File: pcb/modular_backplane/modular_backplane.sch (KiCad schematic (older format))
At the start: 50 parts, among them U1 DMP3028LK3-13, U2 DMP3028LK3-13, U3 PREC002SAAN-RC, U4 NTD4969NT4G, U5 PREC002SAAN-RC, U6 NTD4969NT4G

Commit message: updates
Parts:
- removed boardToCard1, boardToCard2, boardToCard3, boardToCard4, boardToCard5, boardToCard6, boardToCard7, boardToCard8, boardToCard9: SSQ-104-02-T-S-RA, backplane:SSQ-104-02-T-S-RA, symbol backplane_Library:SSQ-104-02-T-S-RA
- added R15, R16: 10K, Resistor_SMD:R_1206_3216Metric_Pad1.42x1.75mm_HandSolder, symbol Device:R
- added boardToCard1, boardToCard2, boardToCard3, boardToCard4, boardToCard5, boardToCard6, boardToCard7, boardToCard8, boardToCard9: SSQ-108-02-T-S-RA, backplane:SSQ-108-02-T-S-RA, symbol backplane_Library:SSQ-108-02-T-S-RA
- added i2cPins1: PREC002SAAN-RC, backplane:PREC002SAAN-RC, symbol backplane_Library:PREC002SAAN-RC
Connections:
- net labels added: scl, sda
- wire segments 229 -> 337
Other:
- note added: "external card connectors"
- note added: "i2c"

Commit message: updates
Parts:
- removed boardToCard1, boardToCard2, boardToCard3, boardToCard4, boardToCard5, boardToCard6, boardToCard7, boardToCard8, boardToCard9: SSQ-108-02-T-S-RA, backplane:SSQ-108-02-T-S-RA, symbol backplane_Library:SSQ-108-02-T-S-RA
- added U7: PREC027DAAN-RC, backplane:PREC027DAAN-RC, symbol backplane_Library:PREC027DAAN-RC
- added card1, card2, card3, card4, card5, card6, card7, card8, card9: PPPC072LJBN-RC, backplane:PPPC072LJBN-RC, symbol backplane_Library:PPPC072LJBN-RC
- R15, R16: value 10K -> 4.7K
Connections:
- net labels added: header1Gpio1, header1Gpio2, header1Gpio3, header1Gpio4, header1Gpio5, header1Gpio6, header2Gpio1, header2Gpio2, header2Gpio3, header2Gpio4, header2Gpio5, header2Gpio6, header3Gpio1, header3Gpio2, header3Gpio3, header3Gpio4, header3Gpio5, header3Gpio6, header4Gpio1, header4Gpio2, header4Gpio3, header4Gpio4, header4Gpio5, header4Gpio6, header5Gpio1, header5Gpio2, header5Gpio3, header5Gpio4, header5Gpio5, header5Gpio6, header6Gpio1, header6Gpio2, header6Gpio3, header6Gpio4, header6Gpio5, header6Gpio6, header7Gpio1, header7Gpio2, header7Gpio3, header7Gpio4, header7Gpio5, header7Gpio6, header8Gpio1, header8Gpio2, header8Gpio3, header8Gpio4, header8Gpio5, header8Gpio6, header9Gpio1, header9Gpio2, header9Gpio3, header9Gpio4, header9Gpio5, header9Gpio6
- wire segments 337 -> 481

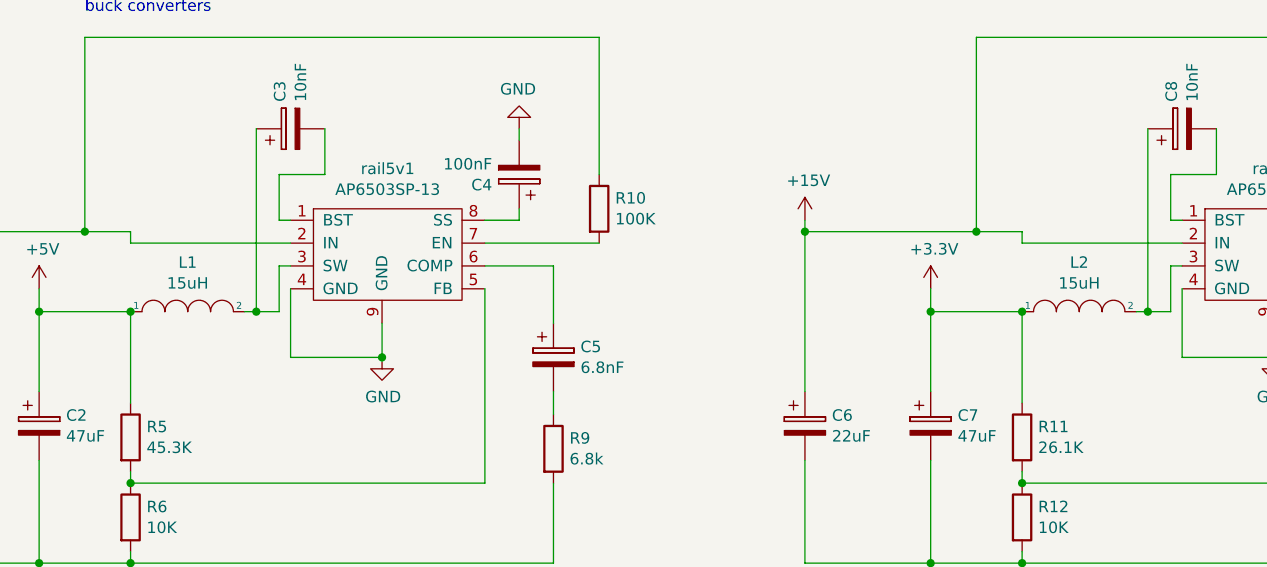
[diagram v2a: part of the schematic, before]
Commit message: layers
i added plane layers to prepare for routing
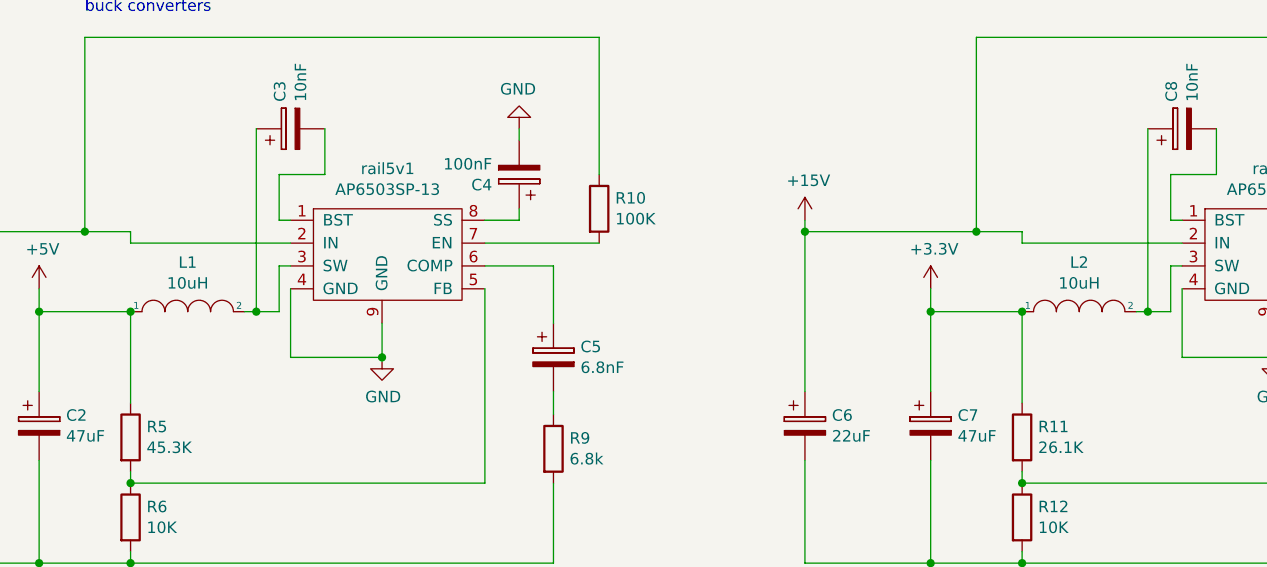
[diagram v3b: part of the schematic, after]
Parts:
- L1, L2: value 15uH -> 10uH; footprint backplane:6100-150K-RC -> backplane:RCH8011NP-100L
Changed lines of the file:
@@
 P 4900 2050
 F 0 "L1" H 4900 2265 50  0000 C CNN
-F 1 "15uH" H 4900 2174 50  0000 C CNN
-F 2 "backplane:6100-150K-RC" H 4900 2050 50  0001 C CNN
+F 1 "10uH" H 4900 2174 50  0000 C CNN
+F 2 "backplane:RCH8011NP-100L" H 4900 2050 50  0001 C CNN
 F 3 "~" H 4900 2050 50  0001 C CNN
 	1    4900 2050
@@
 P 8800 2050
 F 0 "L2" H 8800 2265 50  0000 C CNN
-F 1 "15uH" H 8800 2174 50  0000 C CNN
-F 2 "backplane:6100-150K-RC" H 8800 2050 50  0001 C CNN
+F 1 "10uH" H 8800 2174 50  0000 C CNN
+F 2 "backplane:RCH8011NP-100L" H 8800 2050 50  0001 C CNN
 F 3 "~" H 8800 2050 50  0001 C CNN
 	1    8800 2050

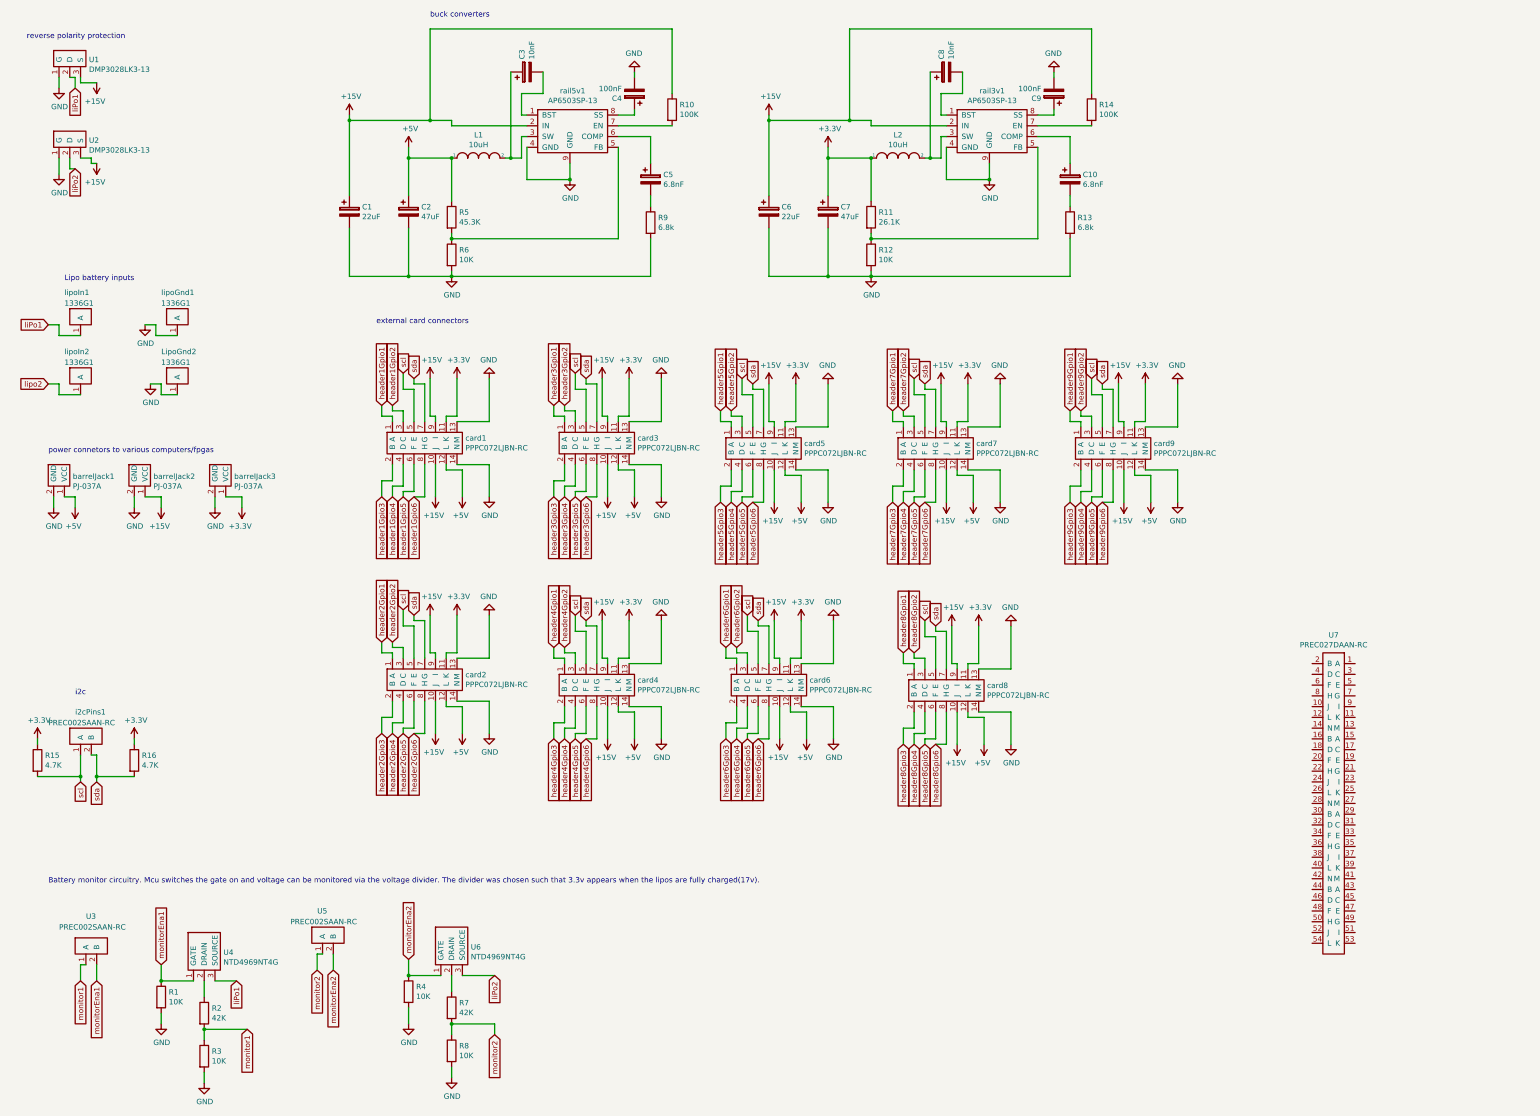
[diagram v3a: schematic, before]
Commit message: added 12v line
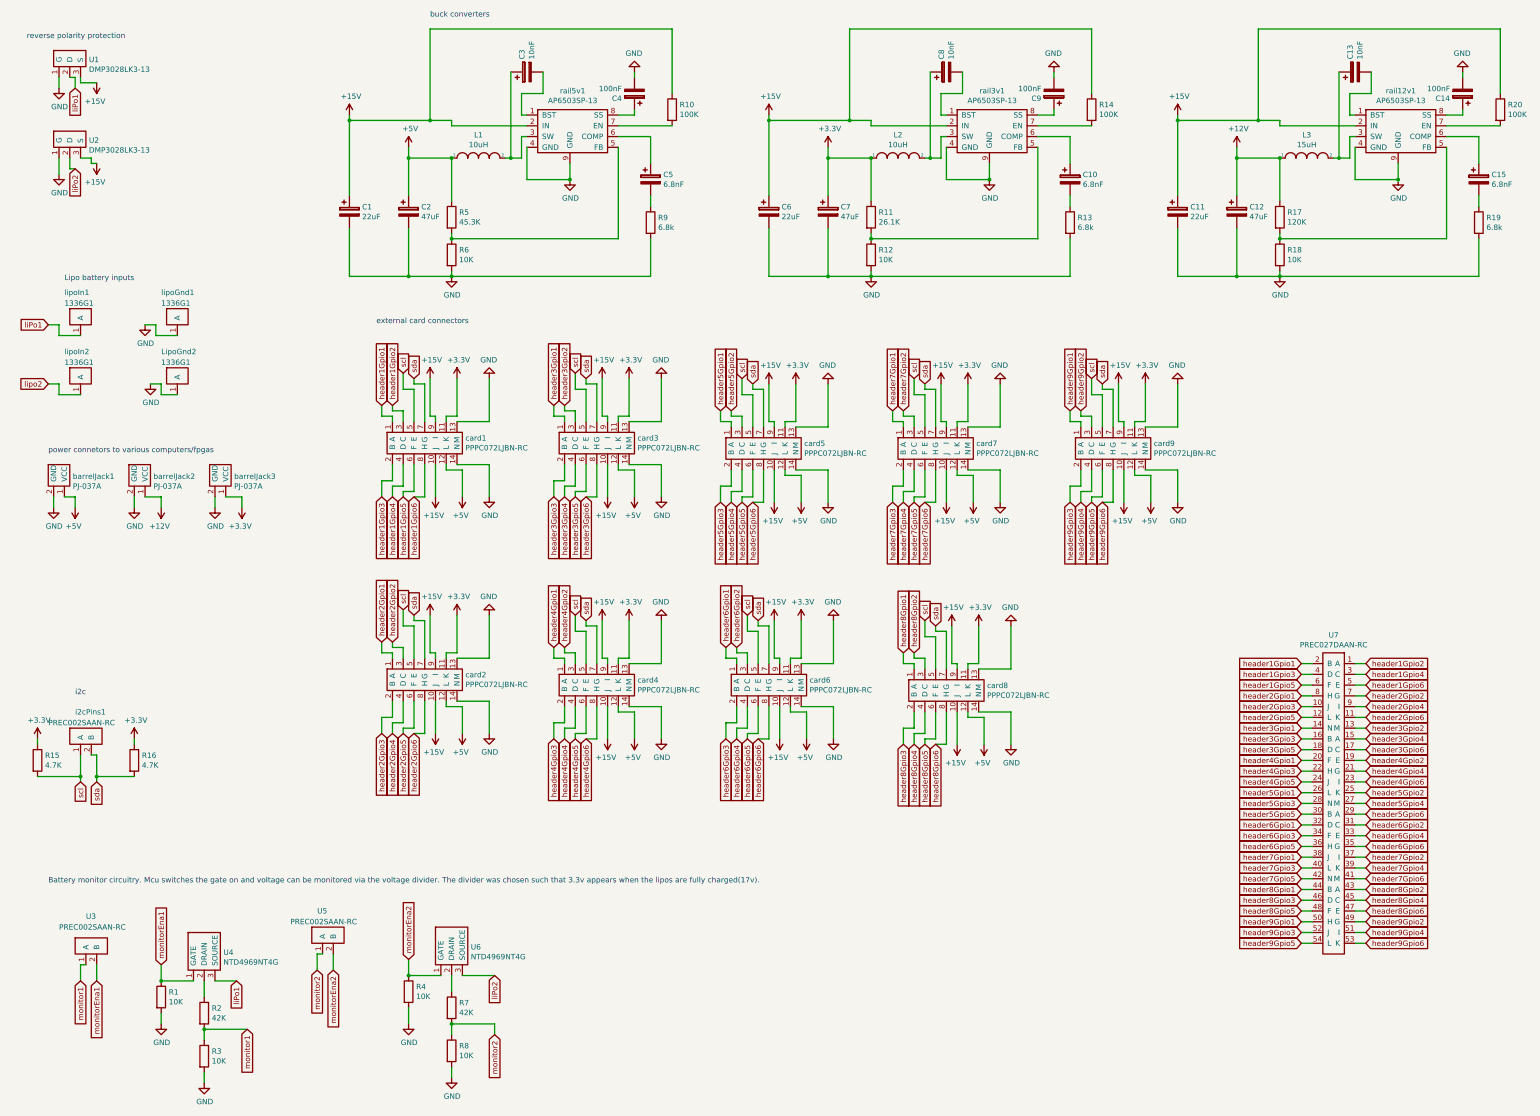
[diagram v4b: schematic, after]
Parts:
- added C11: 22uF, backplane:865090442004, symbol Device:CP
- added C12: 47uF, backplane:865090449007, symbol Device:CP
- added C13: 10nF, Capacitor_SMD:C_1206_3216Metric_Pad1.42x1.75mm_HandSolder, symbol Device:CP
- added C14: 100nF, Capacitor_SMD:C_1206_3216Metric_Pad1.42x1.75mm_HandSolder, symbol Device:CP
- added C15: 6.8nF, Capacitor_SMD:C_1206_3216Metric_Pad1.42x1.75mm_HandSolder, symbol Device:CP
- added L3: 15uH, backplane:6100-150K-RC, symbol pspice:INDUCTOR
- added R17: 120K, Resistor_SMD:R_1206_3216Metric_Pad1.42x1.75mm_HandSolder, symbol Device:R
- added R18: 10K, Resistor_SMD:R_1206_3216Metric_Pad1.42x1.75mm_HandSolder, symbol Device:R
- added R19: 6.8k, Resistor_SMD:R_1206_3216Metric_Pad1.42x1.75mm_HandSolder, symbol Device:R
- added R20: 100K, Resistor_SMD:R_1206_3216Metric_Pad1.42x1.75mm_HandSolder, symbol Device:R
- added rail12v1: AP6503SP-13, backplane:AP6503SP-13, symbol backplane_Library:AP6503SP-13
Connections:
- net +15V: now also C11.1, R20.1, rail12v1.2 (IN); no longer barrelJack2.1 (VCC)
- net GND: now also C11.2, C12.2, C14.2, R18.2, R19.2, rail12v1.4 (GND), rail12v1.9 (GND)
- net header1Gpio1: now also U7.2 (B)
- net header1Gpio2: now also U7.1 (A)
- net header1Gpio3: now also U7.4 (D)
- net header1Gpio4: now also U7.3 (C)
- net header1Gpio5: now also U7.6 (F)
- net header1Gpio6: now also U7.5 (E)
- net header2Gpio1: now also U7.8 (H)
- net header2Gpio2: now also U7.7 (G)
- net header2Gpio3: now also U7.10 (J)
- net header2Gpio4: now also U7.9 (I)
- net header2Gpio5: now also U7.12 (L)
- net header2Gpio6: now also U7.11 (K)
- net header3Gpio1: now also U7.14 (N)
- net header3Gpio2: now also U7.13 (M)
- net header3Gpio3: now also U7.16 (B)
- net header3Gpio4: now also U7.15 (A)
- net header3Gpio5: now also U7.18 (D)
- net header3Gpio6: now also U7.17 (C)
- net header4Gpio1: now also U7.20 (F)
- net header4Gpio2: now also U7.19 (E)
- net header4Gpio3: now also U7.22 (H)
- net header4Gpio4: now also U7.21 (G)
- net header4Gpio5: now also U7.24 (J)
- net header4Gpio6: now also U7.23 (I)
- net header5Gpio1: now also U7.26 (L)
- net header5Gpio2: now also U7.25 (K)
- net header5Gpio3: now also U7.28 (N)
- net header5Gpio4: now also U7.27 (M)
- net header5Gpio5: now also U7.30 (B)
- net header5Gpio6: now also U7.29 (A)
- net header6Gpio1: now also U7.32 (D)
- net header6Gpio2: now also U7.31 (C)
- net header6Gpio3: now also U7.34 (F)
- net header6Gpio4: now also U7.33 (E)
- net header6Gpio5: now also U7.36 (H)
- net header6Gpio6: now also U7.35 (G)
- net header7Gpio1: now also U7.38 (J)
- net header7Gpio2: now also U7.37 (I)
- net header7Gpio3: now also U7.40 (L)
- net header7Gpio4: now also U7.39 (K)
- net header7Gpio5: now also U7.42 (N)
- net header7Gpio6: now also U7.41 (M)
- net header8Gpio1: now also U7.44 (B)
- net header8Gpio2: now also U7.43 (A)
- net header8Gpio3: now also U7.46 (D)
- net header8Gpio4: now also U7.45 (C)
- net header8Gpio5: now also U7.48 (F)
- net header8Gpio6: now also U7.47 (E)
- net header9Gpio1: now also U7.50 (H)
- net header9Gpio2: now also U7.49 (G)
- net header9Gpio3: now also U7.52 (J)
- net header9Gpio4: now also U7.51 (I)
- net header9Gpio5: now also U7.54 (L)
- net header9Gpio6: now also U7.53 (K)
- new net: C13.2, rail12v1.1 (BST)
- new net: C13.1, L3.2, rail12v1.3 (SW)
- new net: R17.2, R18.1, rail12v1.5 (FB)
- new net: C15.1, rail12v1.6 (COMP)
- new net: R20.2, rail12v1.7 (EN)
- new net: C14.1, rail12v1.8 (SS)
- new net: C15.2, R19.1
- new net +12V: C12.1, L3.1, R17.1, barrelJack2.1 (VCC)

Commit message: done
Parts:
- removed R4, R8: 10K, Resistor_SMD:R_1206_3216Metric_Pad1.42x1.75mm_HandSolder, symbol Device:R
- removed R7: 42K, Resistor_SMD:R_1206_3216Metric_Pad1.42x1.75mm_HandSolder, symbol Device:R
- removed U5: PREC002SAAN-RC, backplane:PREC002SAAN-RC, symbol backplane_Library:PREC002SAAN-RC
- removed U6: NTD4969NT4G, backplane:NTD4969NT4G, symbol backplane_Library:NTD4969NT4G
- removed U7: PREC027DAAN-RC, backplane:PREC027DAAN-RC, symbol backplane_Library:PREC027DAAN-RC
- removed card1: PPPC072LJBN-RC, backplane:PPPC072LJBN-RC, symbol backplane_Library:PPPC072LJBN-RC
- added U5: PREC024DAAN-RC, backplane:PREC024DAAN-RC, symbol backplane_Library:PREC024DAAN-RC
- L3: value 15uH -> 10uH; footprint backplane:6100-150K-RC -> backplane:RCH8011NP-100L
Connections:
- net lipo2 is gone; now on net liPo2: lipoIn2.1 (A)
- net +15V: now also U4.3 (SOURCE)
- net GND: now also card2.5 (E), card2.7 (G), card3.5 (E), card3.7 (G), card4.5 (E), card4.7 (G), card5.5 (E), card5.7 (G), card6.5 (E), card6.7 (G), card7.5 (E), card7.7 (G), card8.5 (E), card8.7 (G), card9.5 (E), card9.7 (G); no longer card2.13 (M), card2.14 (N), card3.13 (M), card3.14 (N), card4.13 (M), card4.14 (N), card5.13 (M), card5.14 (N), card6.13 (M), card6.14 (N), card7.13 (M), card7.14 (N), card8.13 (M), card8.14 (N), card9.13 (M), card9.14 (N)
- net header2Gpio1: now also U5.10 (J)
- net header2Gpio2: now also U5.12 (L)
- net header2Gpio3: now also U5.8 (H)
- net header2Gpio4: now also U5.6 (F)
- net header2Gpio5: now also U5.4 (D)
- net header2Gpio6: now also U5.2 (B)
- net header3Gpio1: now also U5.22 (H)
- net header3Gpio2: now also U5.24 (J)
- net header3Gpio3: now also U5.20 (F)
- net header3Gpio4: now also U5.18 (D)
- net header3Gpio5: now also U5.16 (B)
- net header3Gpio6: now also U5.14 (N)
- net header4Gpio1: now also U5.34 (F)
- net header4Gpio2: now also U5.36 (H)
- net header4Gpio3: now also U5.32 (D)
- net header4Gpio4: now also U5.30 (B)
- net header4Gpio5: now also U5.28 (N)
- net header4Gpio6: now also U5.26 (L)
- net header5Gpio1: now also U5.46 (D)
- net header5Gpio2: now also U5.48 (F)
- net header5Gpio3: now also U5.44 (B)
- net header5Gpio4: now also U5.42 (N)
- net header5Gpio5: now also U5.40 (L)
- net header5Gpio6: now also U5.38 (J)
- net header6Gpio1: now also U5.3 (C)
- net header6Gpio2: now also U5.1 (A)
- net header6Gpio3: now also U5.5 (E)
- net header6Gpio4: now also U5.7 (G)
- net header6Gpio5: now also U5.9 (I)
- net header6Gpio6: now also U5.11 (K)
- net header7Gpio1: now also U5.15 (A)
- net header7Gpio2: now also U5.13 (M)
- net header7Gpio3: now also U5.17 (C)
- net header7Gpio4: now also U5.19 (E)
- net header7Gpio5: now also U5.21 (G)
- net header7Gpio6: now also U5.23 (I)
- net header8Gpio1: now also U5.27 (M)
- net header8Gpio2: now also U5.25 (K)
- net header8Gpio3: now also U5.29 (A)
- net header8Gpio4: now also U5.31 (C)
- net header8Gpio5: now also U5.33 (E)
- net header8Gpio6: now also U5.35 (G)
- net header9Gpio1: now also U5.39 (K)
- net header9Gpio2: now also U5.37 (I)
- net header9Gpio3: now also U5.41 (M)
- net header9Gpio4: now also U5.43 (A)
- net header9Gpio5: now also U5.45 (C)
- net header9Gpio6: now also U5.47 (E)
- net liPo1: no longer U4.3 (SOURCE)
- net scl: now also card2.14 (N), card3.14 (N), card4.14 (N), card5.14 (N), card6.14 (N), card7.14 (N), card8.14 (N), card9.14 (N); no longer card2.5 (E), card3.5 (E), card4.5 (E), card5.5 (E), card6.5 (E), card7.5 (E), card8.5 (E), card9.5 (E)
- net sda: now also card2.13 (M), card3.13 (M), card4.13 (M), card5.13 (M), card6.13 (M), card7.13 (M), card8.13 (M), card9.13 (M); no longer card2.7 (G), card3.7 (G), card4.7 (G), card5.7 (G), card6.7 (G), card7.7 (G), card8.7 (G), card9.7 (G)
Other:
- moved on the sheet: card3, card5, card7, card9

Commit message: motordriver finished
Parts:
- added U6, U7, U8, U9: mountingHole, backplane:mountingHole, symbol backplane_Library:mountingHole
- renumbered U3 to monitorPins1
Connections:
- net GND: now also U6.1 (A), U7.1 (A), U8.1 (A), U9.1 (A)
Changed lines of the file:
@@
 Battery monitor circuitry. Mcu switches the gate on and voltage can be monitored via the voltage divider. The divider was chosen such that 3.3v appears when the lipos are fully charged(17v).
 $Comp
-L backplane_Library:PREC002SAAN-RC U3
+L backplane_Library:PREC002SAAN-RC monitorPins1
 U 1 1 5C718C1D
 P 1300 9550
-F 0 "U3" H 1250 10000 50  0000 L CNN
+F 0 "monitorPins1" H 1250 10000 50  0000 L CNN
 F 1 "PREC002SAAN-RC" H 1000 9900 50  0000 L CNN
 F 2 "backplane:PREC002SAAN-RC" H 1300 9550 50  0001 C CNN
@@
 	9150 6350 9150 6450
 Connection ~ 9100 6350
+$Comp
+L backplane_Library:mountingHole U6
+U 1 1 5C4894C8
+P 11050 4100
+F 0 "U6" H 11128 4115 50  0000 L CNN
+F 1 "mountingHole" H 11128 4024 50  0000 L CNN
+F 2 "backplane:mountingHole" H 11050 4100 50  0001 C CNN
+F 3 "" H 11050 4100 50  0001 C CNN
+	1    11050 4100
+	1    0    0    -1
+$EndComp
+$Comp
+L backplane_Library:mountingHole U8
+U 1 1 5C489687
+P 11850 4100
+F 0 "U8" H 11928 4115 50  0000 L CNN
+F 1 "mountingHole" H 11928 4024 50  0000 L CNN
+F 2 "backplane:mountingHole" H 11850 4100 50  0001 C CNN
+F 3 "" H 11850 4100 50  0001 C CNN
+	1    11850 4100
+	1    0    0    -1
+$EndComp
+$Comp
+L backplane_Library:mountingHole U7
+U 1 1 5C4CC57F
+P 11050 4650
+F 0 "U7" H 11128 4665 50  0000 L CNN
+F 1 "mountingHole" H 11128 4574 50  0000 L CNN
+F 2 "backplane:mountingHole" H 11050 4650 50  0001 C CNN
+F 3 "" H 11050 4650 50  0001 C CNN
+	1    11050 4650
+	1    0    0    -1
+$EndComp
+$Comp
+L backplane_Library:mountingHole U9
+U 1 1 5C50F47E
+P 11850 4650
+F 0 "U9" H 11928 4665 50  0000 L CNN
+F 1 "mountingHole" H 11928 4574 50  0000 L CNN
+F 2 "backplane:mountingHole" H 11850 4650 50  0001 C CNN
+F 3 "" H 11850 4650 50  0001 C CNN
+	1    11850 4650
+	1    0    0    -1
+$EndComp
+$Comp
+L power:GND #PWR0101
+U 1 1 5C5527EF
+P 11050 4250
+F 0 "#PWR0101" H 11050 4000 50  0001 C CNN
+F 1 "GND" H 11055 4077 50  0000 C CNN
+F 2 "" H 11050 4250 50  0001 C CNN
+F 3 "" H 11050 4250 50  0001 C CNN
+	1    11050 4250
+	1    0    0    -1
+$EndComp
+$Comp
+L power:GND #PWR0102
+U 1 1 5C55289D
+P 11850 4250
+F 0 "#PWR0102" H 11850 4000 50  0001 C CNN
+F 1 "GND" H 11855 4077 50  0000 C CNN
+F 2 "" H 11850 4250 50  0001 C CNN
+F 3 "" H 11850 4250 50  0001 C CNN
+	1    11850 4250
+	1    0    0    -1
+$EndComp
+$Comp
+L power:GND #PWR0103
+U 1 1 5C55293D
+P 11050 4800
+F 0 "#PWR0103" H 11050 4550 50  0001 C CNN
+F 1 "GND" H 11055 4627 50  0000 C CNN
+F 2 "" H 11050 4800 50  0001 C CNN
+F 3 "" H 11050 4800 50  0001 C CNN
+	1    11050 4800
+	1    0    0    -1
+$EndComp
+$Comp
+L power:GND #PWR0104
+U 1 1 5C5529DD
+P 11850 4800
+F 0 "#PWR0104" H 11850 4550 50  0001 C CNN
+F 1 "GND" H 11855 4627 50  0000 C CNN
+F 2 "" H 11850 4800 50  0001 C CNN
+F 3 "" H 11850 4800 50  0001 C CNN
+	1    11850 4800
+	1    0    0    -1
+$EndComp
 $EndSCHEMATC
